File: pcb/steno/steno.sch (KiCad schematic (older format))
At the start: 61 parts, among them J1 USB_C_Receptacle_USB2.0, K1 PG1350, K10 PG1350, K11 PG1350, K12 PG1350, K13 PG1350, K14 PG1350, K15 PG1350, K16 PG1350, K17 PG1350, K18 PG1350, K19 PG1350, K2 PG1350, K20 PG1350, K21 PG1350, K22 PG1350, K23 PG1350, K24 PG1350, K25 PG1350, K26 PG1350, K27 PG1350, K28 PG1350, K29 PG1350, K3 PG1350, K30 PG1350, K4 PG1350, K5 PG1350, K6 PG1350, K7 PG1350, K8 PG1350, K9 PG1350, SW1 SW_Push, SW2 SW_Push, U1 ATmega32U4-AU, U2 MT25QL128ABA1ESE, U3 MCP1700-3302E_SOT23, U4 LCD2.2in, U5 4050, U6 SRV05-4, Y1 16MHz

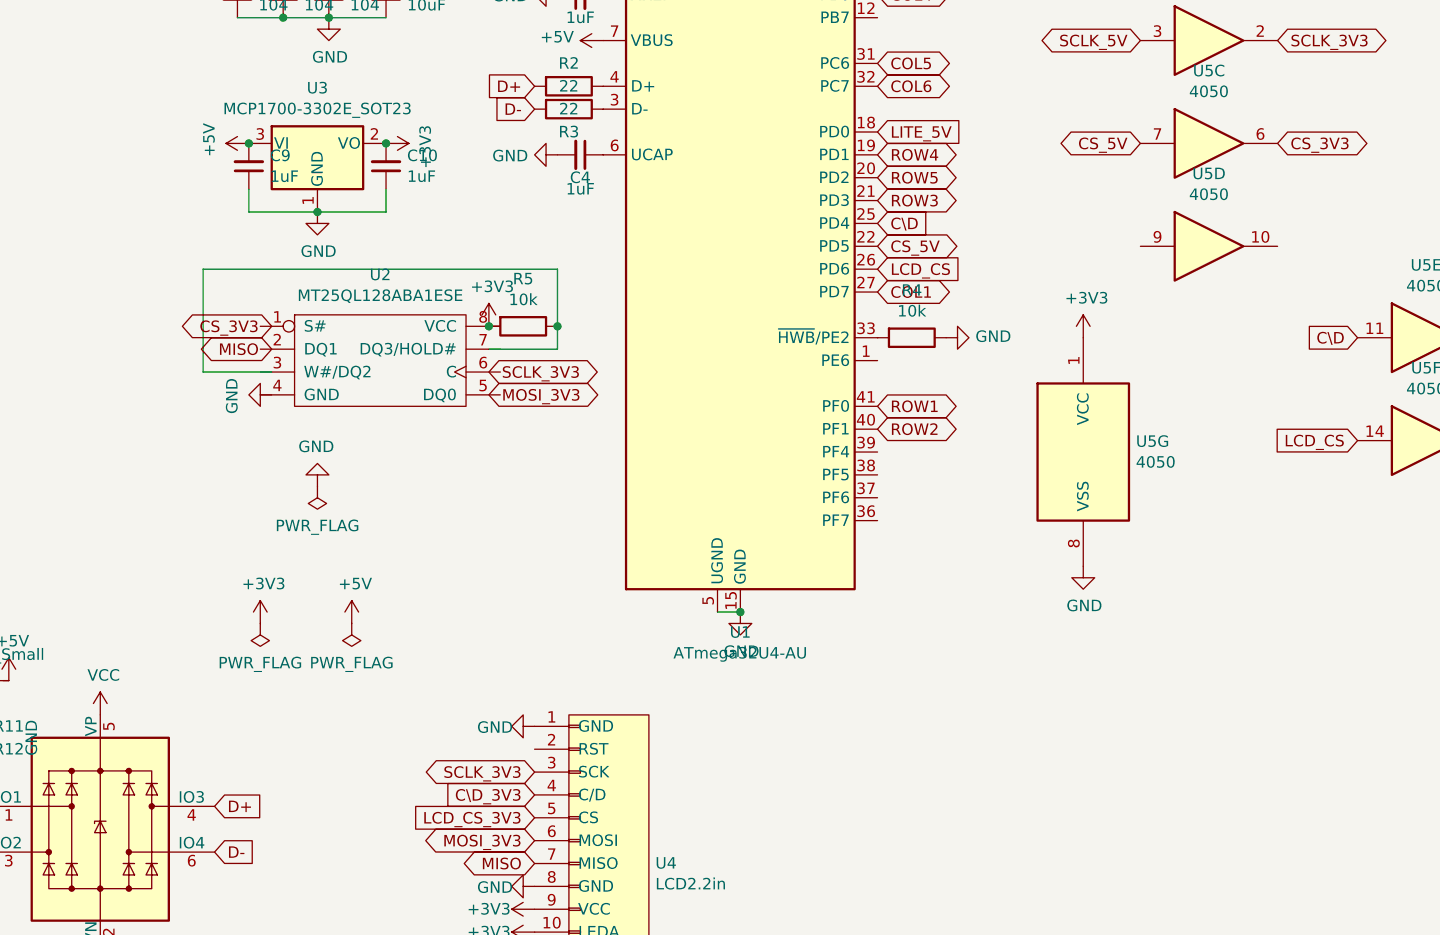
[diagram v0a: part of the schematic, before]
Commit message: [compiler] Add compiled simple rules
- Remove word list cuz we can't use that anywhere
- Compile simple rules (exception from regex rules) into 64KiB sized binary hashmap
- Rules comes from https://github.com/nimble0/dotterel/blob/master/app/src/main/assets/orthography/english.simple.json
- Load rules at `0xF30000`
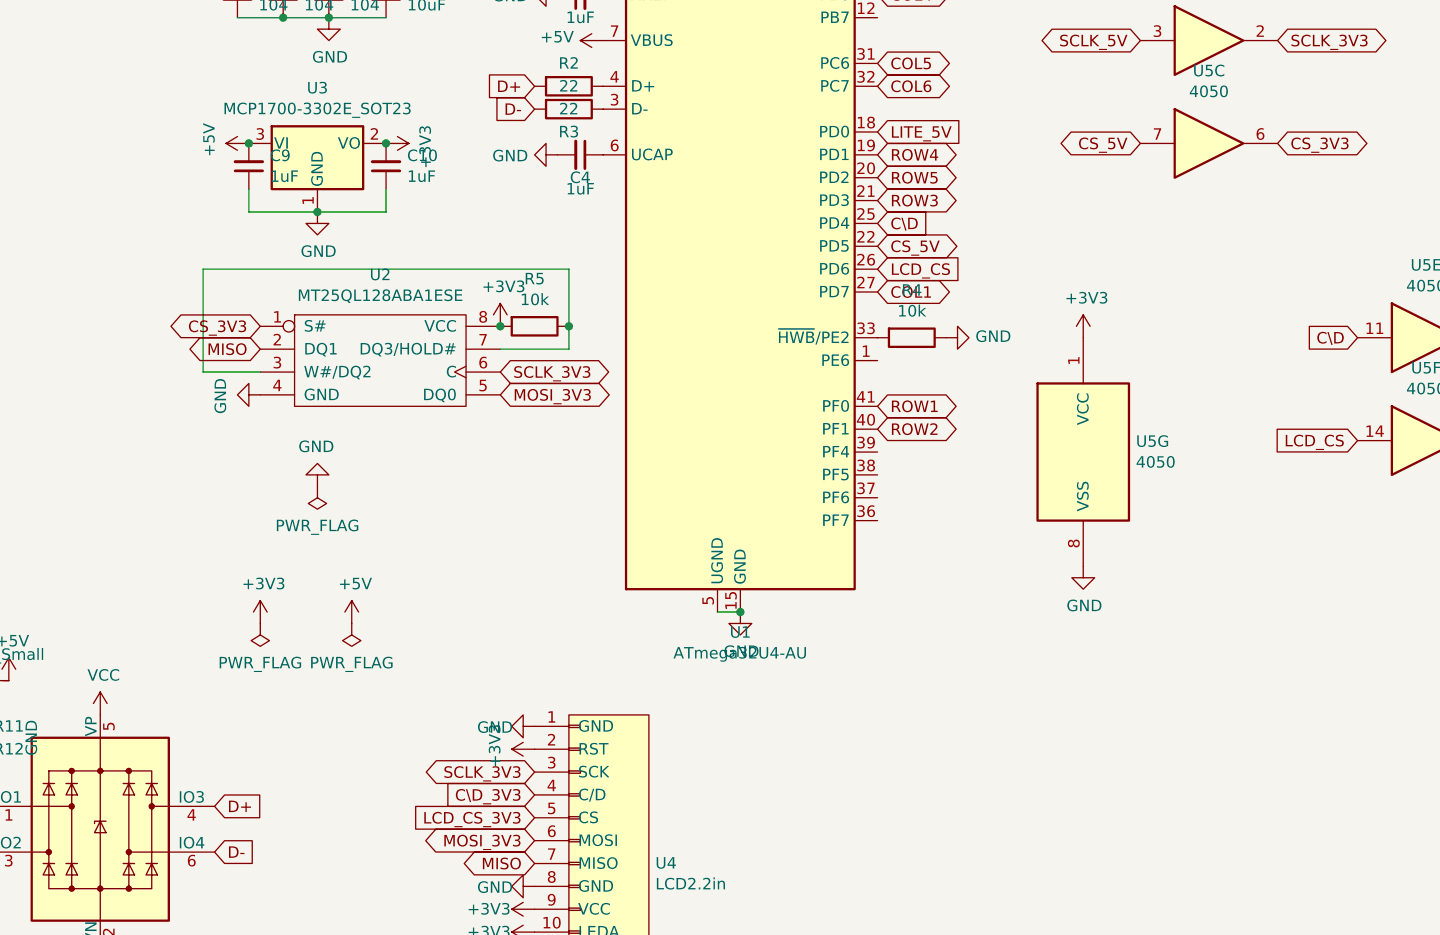
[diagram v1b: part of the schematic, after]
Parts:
- removed unit 4 of U5
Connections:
- net +3V3: now also U2.8 (VCC), U4.2 (RST)
- net CS_3V3: now also U2.1 (S#)
- net GND: now also U2.4 (GND)
- net MISO: now also U2.2 (DQ1)
- net MOSI_3V3: now also U2.5 (DQ0)
- net SCLK_3V3: now also U2.6 (C)
- net at U2.3 (W#/DQ2): now also R5.1, U2.7 (DQ3/HOLD#)
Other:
- moved on the sheet: R5
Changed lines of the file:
@@
 Text GLabel 7850 2600 2    50   BiDi ~ 0
 ROW3
-Text GLabel 6150 3450 2    50   BiDi ~ 0
+Text GLabel 6200 3450 2    50   BiDi ~ 0
 MOSI_3V3
-Text GLabel 5200 3250 0    50   BiDi ~ 0
+Text GLabel 5150 3250 0    50   BiDi ~ 0
 MISO
-Text GLabel 6150 3350 2    50   BiDi ~ 0
+Text GLabel 6200 3350 2    50   BiDi ~ 0
 SCLK_3V3
-Text GLabel 5200 3150 0    50   BiDi ~ 0
+Text GLabel 5150 3150 0    50   BiDi ~ 0
 CS_3V3
 $Comp
@@
 L power:+3V3 #PWR012
 U 1 1 5F718F7E
-P 6150 3150
-F 0 "#PWR012" H 6150 3000 50  0001 C CNN
-F 1 "+3V3" H 6165 3323 50  0000 C CNN
-F 2 "" H 6150 3150 50  0001 C CNN
-F 3 "" H 6150 3150 50  0001 C CNN
-	1    6150 3150
+P 6200 3150
+F 0 "#PWR012" H 6200 3000 50  0001 C CNN
+F 1 "+3V3" H 6215 3323 50  0000 C CNN
+F 2 "" H 6200 3150 50  0001 C CNN
+F 3 "" H 6200 3150 50  0001 C CNN
+	1    6200 3150
 	1    0    0    -1
 $EndComp
@@
 L Device:R R5
 U 1 1 5F8001B1
-P 6300 3150
-F 0 "R5" V 6093 3150 50  0000 C CNN
-F 1 "10k" V 6184 3150 50  0000 C CNN
-F 2 "Resistor_SMD:R_0805_2012Metric" V 6230 3150 50  0001 C CNN
-F 3 "~" H 6300 3150 50  0001 C CNN
-	1    6300 3150
-	0    1    1    0
-$EndComp
-Connection ~ 6150 3150
-Wire Wire Line
-	6450 3150 6450 3250
-Wire Wire Line
-	6450 3250 6150 3250
-Wire Wire Line
-	6450 3150 6450 2900
-Wire Wire Line
-	6450 2900 4900 2900
+P 6350 3150
+F 0 "R5" V 6143 3150 50  0000 C CNN
+F 1 "10k" V 6234 3150 50  0000 C CNN
+F 2 "Resistor_SMD:R_0805_2012Metric" V 6280 3150 50  0001 C CNN
+F 3 "~" H 6350 3150 50  0001 C CNN
+	1    6350 3150
+	0    1    1    0
+$EndComp
 Wire Wire Line
 	4900 2900 4900 3350
-Wire Wire Line
-	4900 3350 5200 3350
-Connection ~ 6450 3150
 Text GLabel 7850 2900 2    50   Input ~ 0
 LCD_CS
@@
 L power:GND #PWR0109
 U 1 1 5F8C4316
-P 5200 3450
-F 0 "#PWR0109" H 5200 3200 50  0001 C CNN
-F 1 "GND" H 5205 3277 50  0000 C CNN
-F 2 "" H 5200 3450 50  0001 C CNN
-F 3 "" H 5200 3450 50  0001 C CNN
-	1    5200 3450
+P 5150 3450
+F 0 "#PWR0109" H 5150 3200 50  0001 C CNN
+F 1 "GND" H 5155 3277 50  0000 C CNN
+F 2 "" H 5150 3450 50  0001 C CNN
+F 3 "" H 5150 3450 50  0001 C CNN
+	1    5150 3450
 	0    1    1    0
 $EndComp
@@
 Wire Wire Line
 	6050 5900 5850 5900
-$Comp
-L 4xxx:4050 U5
-U 4 1 5F93A4B9
-P 9300 2800
-F 0 "U5" H 9300 3117 50  0000 C CNN
-F 1 "4050" H 9300 3026 50  0000 C CNN
-F 2 "Package_SO:SOIC-16_3.9x9.9mm_P1.27mm" H 9300 2800 50  0001 C CNN
-F 3 "http://www.intersil.com/content/dam/intersil/documents/cd40/cd4050bms.pdf" H 9300 2800 50  0001 C CNN
-	4    9300 2800
-	1    0    0    -1
-$EndComp
 Text GLabel 6650 1100 0    50   Input ~ 0
 RESET
@@
 Wire Wire Line
 	3600 5200 3600 5300
+$Comp
+L power:+3V3 #PWR0104
+U 1 1 6057878C
+P 6350 5000
+F 0 "#PWR0104" H 6350 4850 50  0001 C CNN
+F 1 "+3V3" H 6365 5173 50  0000 C CNN
+F 2 "" H 6350 5000 50  0001 C CNN
+F 3 "" H 6350 5000 50  0001 C CNN
+	1    6350 5000
+	0    -1   -1   0
+$EndComp
+Wire Wire Line
+	4900 3350 5150 3350
+Connection ~ 6200 3150
+Wire Wire Line
+	6500 2900 6500 3150
+Wire Wire Line
+	4900 2900 6500 2900
+Wire Wire Line
+	6200 3250 6500 3250
+Wire Wire Line
+	6500 3250 6500 3150
+Connection ~ 6500 3150
 $EndSCHEMATC
